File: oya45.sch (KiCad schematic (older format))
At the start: 94 parts, among them U1 ProMicro

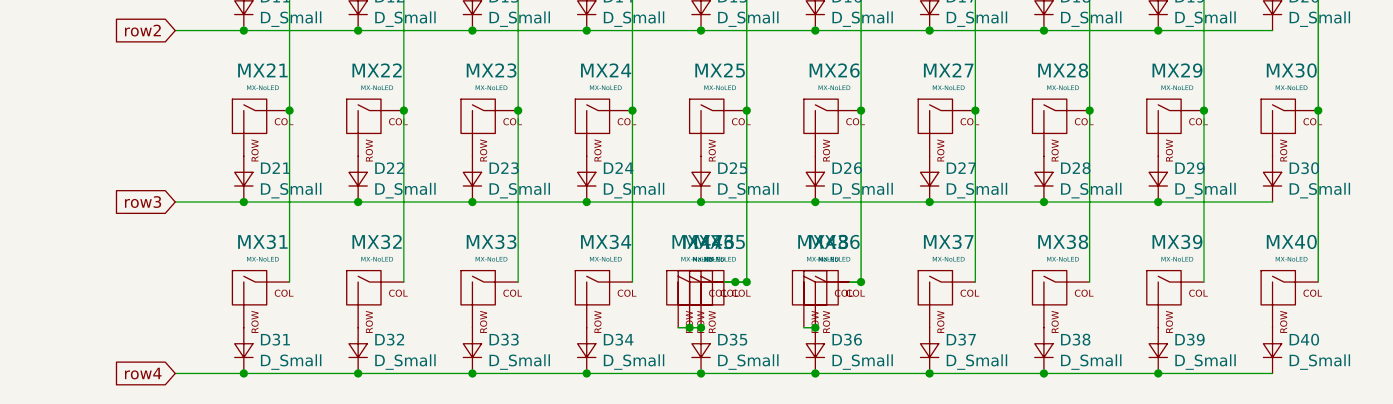
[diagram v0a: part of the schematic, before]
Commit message: schematics update
added bottom row schematics
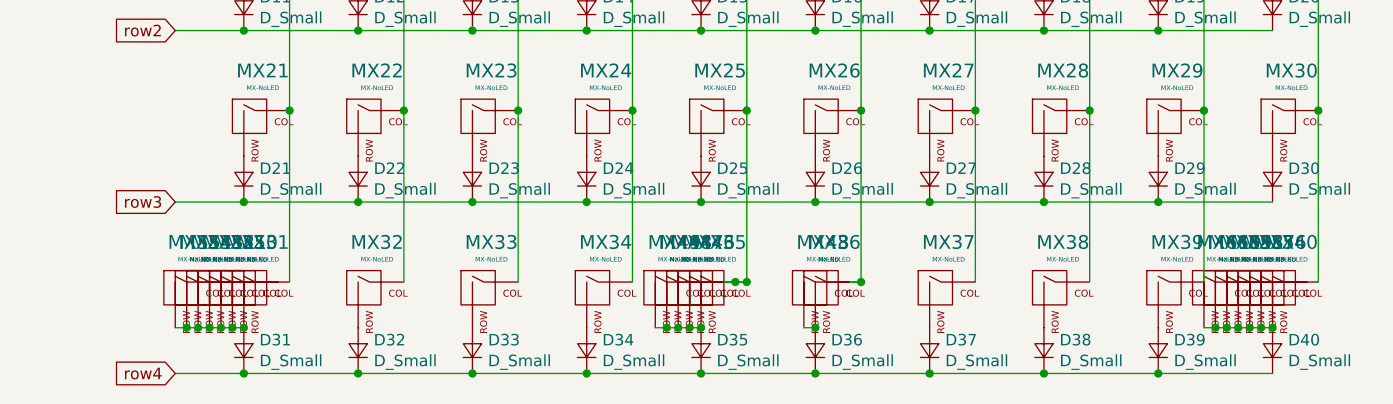
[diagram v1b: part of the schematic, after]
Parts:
- added MX48, MX49: MX-NoLED, MX_Only:MXOnly-2U-ReversedStabilizers-NoLED, symbol MX_Alps_Hybrid:MX-NoLED
- added MX50, MX51, MX52, MX53, MX54, MX55, MX56, MX57, MX58, MX59, MX60, MX61: MX-NoLED, MX_Only:MXOnly-1U-NoLED, symbol MX_Alps_Hybrid:MX-NoLED
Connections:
- net at D31.2 (A), MX31.2 (ROW): now also MX50.2 (ROW), MX51.2 (ROW), MX52.2 (ROW), MX53.2 (ROW), MX54.2 (ROW), MX55.2 (ROW)
- net at D35.2 (A), MX35.2 (ROW), MX46.2 (ROW)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: now also MX48.2 (ROW), MX49.2 (ROW)
- net at D40.2 (A), MX40.2 (ROW): now also MX56.2 (ROW), MX57.2 (ROW), MX58.2 (ROW), MX59.2 (ROW), MX60.2 (ROW), MX61.2 (ROW)
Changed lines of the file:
@@
 	7750 2550 7750 1500
 Connection ~ 7750 2550
+$Comp
+L MX_Alps_Hybrid:MX-NoLED MX50
+U 1 1 6130DEB4
+P 5550 4850
+F 0 "MX50" H 5583 5073 60  0000 C CNN
+F 1 "MX-NoLED" H 5583 4999 20  0000 C CNN
+F 2 "MX_Only:MXOnly-1U-NoLED" H 4925 4825 60  0001 C CNN
+F 3 "" H 4925 4825 60  0001 C CNN
+	1    5550 4850
+	1    0    0    -1
+$EndComp
+$Comp
+L MX_Alps_Hybrid:MX-NoLED MX51
+U 1 1 61310BF7
+P 5500 4850
+F 0 "MX51" H 5533 5073 60  0000 C CNN
+F 1 "MX-NoLED" H 5533 4999 20  0000 C CNN
+F 2 "MX_Only:MXOnly-1U-NoLED" H 4875 4825 60  0001 C CNN
+F 3 "" H 4875 4825 60  0001 C CNN
+	1    5500 4850
+	1    0    0    -1
+$EndComp
+$Comp
+L MX_Alps_Hybrid:MX-NoLED MX52
+U 1 1 6131191D
+P 5450 4850
+F 0 "MX52" H 5483 5073 60  0000 C CNN
+F 1 "MX-NoLED" H 5483 4999 20  0000 C CNN
+F 2 "MX_Only:MXOnly-1U-NoLED" H 4825 4825 60  0001 C CNN
+F 3 "" H 4825 4825 60  0001 C CNN
+	1    5450 4850
+	1    0    0    -1
+$EndComp
+$Comp
+L MX_Alps_Hybrid:MX-NoLED MX53
+U 1 1 61311AAE
+P 5400 4850
+F 0 "MX53" H 5433 5073 60  0000 C CNN
+F 1 "MX-NoLED" H 5433 4999 20  0000 C CNN
+F 2 "MX_Only:MXOnly-1U-NoLED" H 4775 4825 60  0001 C CNN
+F 3 "" H 4775 4825 60  0001 C CNN
+	1    5400 4850
+	1    0    0    -1
+$EndComp
+$Comp
+L MX_Alps_Hybrid:MX-NoLED MX54
+U 1 1 61311CE4
+P 5350 4850
+F 0 "MX54" H 5383 5073 60  0000 C CNN
+F 1 "MX-NoLED" H 5383 4999 20  0000 C CNN
+F 2 "MX_Only:MXOnly-1U-NoLED" H 4725 4825 60  0001 C CNN
+F 3 "" H 4725 4825 60  0001 C CNN
+	1    5350 4850
+	1    0    0    -1
+$EndComp
+$Comp
+L MX_Alps_Hybrid:MX-NoLED MX55
+U 1 1 61311E89
+P 5300 4850
+F 0 "MX55" H 5333 5073 60  0000 C CNN
+F 1 "MX-NoLED" H 5333 4999 20  0000 C CNN
+F 2 "MX_Only:MXOnly-1U-NoLED" H 4675 4825 60  0001 C CNN
+F 3 "" H 4675 4825 60  0001 C CNN
+	1    5300 4850
+	1    0    0    -1
+$EndComp
+$Comp
+L MX_Alps_Hybrid:MX-NoLED MX56
+U 1 1 6131203D
+P 10050 4850
+F 0 "MX56" H 10083 5073 60  0000 C CNN
+F 1 "MX-NoLED" H 10083 4999 20  0000 C CNN
+F 2 "MX_Only:MXOnly-1U-NoLED" H 9425 4825 60  0001 C CNN
+F 3 "" H 9425 4825 60  0001 C CNN
+	1    10050 4850
+	1    0    0    -1
+$EndComp
+$Comp
+L MX_Alps_Hybrid:MX-NoLED MX57
+U 1 1 6131231D
+P 10000 4850
+F 0 "MX57" H 10033 5073 60  0000 C CNN
+F 1 "MX-NoLED" H 10033 4999 20  0000 C CNN
+F 2 "MX_Only:MXOnly-1U-NoLED" H 9375 4825 60  0001 C CNN
+F 3 "" H 9375 4825 60  0001 C CNN
+	1    10000 4850
+	1    0    0    -1
+$EndComp
+$Comp
+L MX_Alps_Hybrid:MX-NoLED MX58
+U 1 1 6131254E
+P 9950 4850
+F 0 "MX58" H 9983 5073 60  0000 C CNN
+F 1 "MX-NoLED" H 9983 4999 20  0000 C CNN
+F 2 "MX_Only:MXOnly-1U-NoLED" H 9325 4825 60  0001 C CNN
+F 3 "" H 9325 4825 60  0001 C CNN
+	1    9950 4850
+	1    0    0    -1
+$EndComp
+$Comp
+L MX_Alps_Hybrid:MX-NoLED MX59
+U 1 1 6131279D
+P 9900 4850
+F 0 "MX59" H 9933 5073 60  0000 C CNN
+F 1 "MX-NoLED" H 9933 4999 20  0000 C CNN
+F 2 "MX_Only:MXOnly-1U-NoLED" H 9275 4825 60  0001 C CNN
+F 3 "" H 9275 4825 60  0001 C CNN
+	1    9900 4850
+	1    0    0    -1
+$EndComp
+$Comp
+L MX_Alps_Hybrid:MX-NoLED MX60
+U 1 1 613129F6
+P 9850 4850
+F 0 "MX60" H 9883 5073 60  0000 C CNN
+F 1 "MX-NoLED" H 9883 4999 20  0000 C CNN
+F 2 "MX_Only:MXOnly-1U-NoLED" H 9225 4825 60  0001 C CNN
+F 3 "" H 9225 4825 60  0001 C CNN
+	1    9850 4850
+	1    0    0    -1
+$EndComp
+$Comp
+L MX_Alps_Hybrid:MX-NoLED MX61
+U 1 1 61312BF5
+P 9800 4850
+F 0 "MX61" H 9833 5073 60  0000 C CNN
+F 1 "MX-NoLED" H 9833 4999 20  0000 C CNN
+F 2 "MX_Only:MXOnly-1U-NoLED" H 9175 4825 60  0001 C CNN
+F 3 "" H 9175 4825 60  0001 C CNN
+	1    9800 4850
+	1    0    0    -1
+$EndComp
+$Comp
+L MX_Alps_Hybrid:MX-NoLED MX48
+U 1 1 61316CF3
+P 7450 4850
+F 0 "MX48" H 7483 5073 60  0000 C CNN
+F 1 "MX-NoLED" H 7483 4999 20  0000 C CNN
+F 2 "MX_Only:MXOnly-2U-ReversedStabilizers-NoLED" H 6825 4825 60  0001 C CNN
+F 3 "" H 6825 4825 60  0001 C CNN
+	1    7450 4850
+	1    0    0    -1
+$EndComp
+$Comp
+L MX_Alps_Hybrid:MX-NoLED MX49
+U 1 1 61316F9C
+P 7400 4850
+F 0 "MX49" H 7433 5073 60  0000 C CNN
+F 1 "MX-NoLED" H 7433 4999 20  0000 C CNN
+F 2 "MX_Only:MXOnly-2U-ReversedStabilizers-NoLED" H 6775 4825 60  0001 C CNN
+F 3 "" H 6775 4825 60  0001 C CNN
+	1    7400 4850
+	1    0    0    -1
+$EndComp
+Wire Wire Line
+	7450 5000 7400 5000
+Connection ~ 7450 5000
+Connection ~ 7400 5000
+Wire Wire Line
+	7400 5000 7350 5000
+Connection ~ 5550 5000
+Wire Wire Line
+	5300 5000 5250 5000
+Connection ~ 5300 5000
+Wire Wire Line
+	5350 5000 5300 5000
+Connection ~ 5350 5000
+Wire Wire Line
+	5400 5000 5350 5000
+Connection ~ 5400 5000
+Wire Wire Line
+	5450 5000 5400 5000
+Connection ~ 5450 5000
+Wire Wire Line
+	5550 5000 5500 5000
+Wire Wire Line
+	5500 5000 5450 5000
+Connection ~ 5500 5000
+Connection ~ 10050 5000
+Wire Wire Line
+	9800 5000 9750 5000
+Connection ~ 9800 5000
+Wire Wire Line
+	9850 5000 9800 5000
+Connection ~ 9850 5000
+Wire Wire Line
+	9900 5000 9850 5000
+Connection ~ 9900 5000
+Wire Wire Line
+	9950 5000 9900 5000
+Connection ~ 9950 5000
+Wire Wire Line
+	10050 5000 10000 5000
+Wire Wire Line
+	10000 5000 9950 5000
+Connection ~ 10000 5000
 $EndSCHEMATC

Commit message: fixed schematic
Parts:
- renumbered MX48 to MX49, MX49 to MX50, MX50 to MX51, MX51 to MX52, MX52 to MX53, MX53 to MX54, MX54 to MX55, MX55 to MX56, MX56 to MX57, MX57 to MX58, MX58 to MX59, MX59 to MX60, MX60 to MX61, MX61 to MX62
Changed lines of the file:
@@
 Connection ~ 7750 2550
 $Comp
-L MX_Alps_Hybrid:MX-NoLED MX50
-U 1 1 6130DEB4
-P 5550 4850
-F 0 "MX50" H 5583 5073 60  0000 C CNN
-F 1 "MX-NoLED" H 5583 4999 20  0000 C CNN
-F 2 "MX_Only:MXOnly-1U-NoLED" H 4925 4825 60  0001 C CNN
-F 3 "" H 4925 4825 60  0001 C CNN
-	1    5550 4850
-	1    0    0    -1
-$EndComp
-$Comp
-L MX_Alps_Hybrid:MX-NoLED MX51
-U 1 1 61310BF7
-P 5500 4850
-F 0 "MX51" H 5533 5073 60  0000 C CNN
-F 1 "MX-NoLED" H 5533 4999 20  0000 C CNN
-F 2 "MX_Only:MXOnly-1U-NoLED" H 4875 4825 60  0001 C CNN
-F 3 "" H 4875 4825 60  0001 C CNN
-	1    5500 4850
-	1    0    0    -1
-$EndComp
-$Comp
-L MX_Alps_Hybrid:MX-NoLED MX52
-U 1 1 6131191D
-P 5450 4850
-F 0 "MX52" H 5483 5073 60  0000 C CNN
-F 1 "MX-NoLED" H 5483 4999 20  0000 C CNN
-F 2 "MX_Only:MXOnly-1U-NoLED" H 4825 4825 60  0001 C CNN
-F 3 "" H 4825 4825 60  0001 C CNN
-	1    5450 4850
-	1    0    0    -1
-$EndComp
-$Comp
-L MX_Alps_Hybrid:MX-NoLED MX53
+L MX_Alps_Hybrid:MX-NoLED MX54
 U 1 1 61311AAE
 P 5400 4850
-F 0 "MX53" H 5433 5073 60  0000 C CNN
+F 0 "MX54" H 5433 5073 60  0000 C CNN
 F 1 "MX-NoLED" H 5433 4999 20  0000 C CNN
 F 2 "MX_Only:MXOnly-1U-NoLED" H 4775 4825 60  0001 C CNN
@@
 $EndComp
 $Comp
-L MX_Alps_Hybrid:MX-NoLED MX54
+L MX_Alps_Hybrid:MX-NoLED MX55
 U 1 1 61311CE4
 P 5350 4850
-F 0 "MX54" H 5383 5073 60  0000 C CNN
+F 0 "MX55" H 5383 5073 60  0000 C CNN
 F 1 "MX-NoLED" H 5383 4999 20  0000 C CNN
 F 2 "MX_Only:MXOnly-1U-NoLED" H 4725 4825 60  0001 C CNN
@@
 $EndComp
 $Comp
-L MX_Alps_Hybrid:MX-NoLED MX55
+L MX_Alps_Hybrid:MX-NoLED MX56
 U 1 1 61311E89
 P 5300 4850
-F 0 "MX55" H 5333 5073 60  0000 C CNN
+F 0 "MX56" H 5333 5073 60  0000 C CNN
 F 1 "MX-NoLED" H 5333 4999 20  0000 C CNN
 F 2 "MX_Only:MXOnly-1U-NoLED" H 4675 4825 60  0001 C CNN
@@
 $EndComp
 $Comp
-L MX_Alps_Hybrid:MX-NoLED MX56
+L MX_Alps_Hybrid:MX-NoLED MX57
 U 1 1 6131203D
 P 10050 4850
-F 0 "MX56" H 10083 5073 60  0000 C CNN
+F 0 "MX57" H 10083 5073 60  0000 C CNN
 F 1 "MX-NoLED" H 10083 4999 20  0000 C CNN
 F 2 "MX_Only:MXOnly-1U-NoLED" H 9425 4825 60  0001 C CNN
@@
 $EndComp
 $Comp
-L MX_Alps_Hybrid:MX-NoLED MX57
+L MX_Alps_Hybrid:MX-NoLED MX58
 U 1 1 6131231D
 P 10000 4850
-F 0 "MX57" H 10033 5073 60  0000 C CNN
+F 0 "MX58" H 10033 5073 60  0000 C CNN
 F 1 "MX-NoLED" H 10033 4999 20  0000 C CNN
 F 2 "MX_Only:MXOnly-1U-NoLED" H 9375 4825 60  0001 C CNN
@@
 $EndComp
 $Comp
-L MX_Alps_Hybrid:MX-NoLED MX58
+L MX_Alps_Hybrid:MX-NoLED MX59
 U 1 1 6131254E
 P 9950 4850
-F 0 "MX58" H 9983 5073 60  0000 C CNN
+F 0 "MX59" H 9983 5073 60  0000 C CNN
 F 1 "MX-NoLED" H 9983 4999 20  0000 C CNN
 F 2 "MX_Only:MXOnly-1U-NoLED" H 9325 4825 60  0001 C CNN
@@
 $EndComp
 $Comp
-L MX_Alps_Hybrid:MX-NoLED MX59
+L MX_Alps_Hybrid:MX-NoLED MX60
 U 1 1 6131279D
 P 9900 4850
-F 0 "MX59" H 9933 5073 60  0000 C CNN
+F 0 "MX60" H 9933 5073 60  0000 C CNN
 F 1 "MX-NoLED" H 9933 4999 20  0000 C CNN
 F 2 "MX_Only:MXOnly-1U-NoLED" H 9275 4825 60  0001 C CNN
@@
 $EndComp
 $Comp
-L MX_Alps_Hybrid:MX-NoLED MX60
+L MX_Alps_Hybrid:MX-NoLED MX61
 U 1 1 613129F6
 P 9850 4850
-F 0 "MX60" H 9883 5073 60  0000 C CNN
+F 0 "MX61" H 9883 5073 60  0000 C CNN
 F 1 "MX-NoLED" H 9883 4999 20  0000 C CNN
 F 2 "MX_Only:MXOnly-1U-NoLED" H 9225 4825 60  0001 C CNN
@@
 $EndComp
 $Comp
-L MX_Alps_Hybrid:MX-NoLED MX61
+L MX_Alps_Hybrid:MX-NoLED MX62
 U 1 1 61312BF5
 P 9800 4850
-F 0 "MX61" H 9833 5073 60  0000 C CNN
+F 0 "MX62" H 9833 5073 60  0000 C CNN
 F 1 "MX-NoLED" H 9833 4999 20  0000 C CNN
 F 2 "MX_Only:MXOnly-1U-NoLED" H 9175 4825 60  0001 C CNN
@@
 $EndComp
 $Comp
-L MX_Alps_Hybrid:MX-NoLED MX48
+L MX_Alps_Hybrid:MX-NoLED MX49
 U 1 1 61316CF3
 P 7450 4850
-F 0 "MX48" H 7483 5073 60  0000 C CNN
+F 0 "MX49" H 7483 5073 60  0000 C CNN
 F 1 "MX-NoLED" H 7483 4999 20  0000 C CNN
 F 2 "MX_Only:MXOnly-2U-ReversedStabilizers-NoLED" H 6825 4825 60  0001 C CNN
@@
 $EndComp
 $Comp
-L MX_Alps_Hybrid:MX-NoLED MX49
+L MX_Alps_Hybrid:MX-NoLED MX50
 U 1 1 61316F9C
 P 7400 4850
-F 0 "MX49" H 7433 5073 60  0000 C CNN
+F 0 "MX50" H 7433 5073 60  0000 C CNN
 F 1 "MX-NoLED" H 7433 4999 20  0000 C CNN
 F 2 "MX_Only:MXOnly-2U-ReversedStabilizers-NoLED" H 6775 4825 60  0001 C CNN
@@
 Wire Wire Line
 	7400 5000 7350 5000
-Connection ~ 5550 5000
 Wire Wire Line
 	5300 5000 5250 5000
@@
 	5400 5000 5350 5000
 Connection ~ 5400 5000
-Wire Wire Line
-	5450 5000 5400 5000
-Connection ~ 5450 5000
-Wire Wire Line
-	5550 5000 5500 5000
-Wire Wire Line
-	5500 5000 5450 5000
-Connection ~ 5500 5000
 Connection ~ 10050 5000
 Wire Wire Line
@@
 	10000 5000 9950 5000
 Connection ~ 10000 5000
+Connection ~ 5550 5000
+Connection ~ 5450 5000
+Wire Wire Line
+	5450 5000 5400 5000
+$Comp
+L MX_Alps_Hybrid:MX-NoLED MX52
+U 1 1 61310BF7
+P 5500 4850
+F 0 "MX52" H 5533 5073 60  0000 C CNN
+F 1 "MX-NoLED" H 5533 4999 20  0000 C CNN
+F 2 "MX_Only:MXOnly-1U-NoLED" H 4875 4825 60  0001 C CNN
+F 3 "" H 4875 4825 60  0001 C CNN
+	1    5500 4850
+	1    0    0    -1
+$EndComp
+Connection ~ 5500 5000
+Wire Wire Line
+	5500 5000 5450 5000
+Wire Wire Line
+	5550 5000 5500 5000
+$Comp
+L MX_Alps_Hybrid:MX-NoLED MX51
+U 1 1 6130DEB4
+P 5550 4850
+F 0 "MX51" H 5583 5073 60  0000 C CNN
+F 1 "MX-NoLED" H 5583 4999 20  0000 C CNN
+F 2 "MX_Only:MXOnly-1U-NoLED" H 4925 4825 60  0001 C CNN
+F 3 "" H 4925 4825 60  0001 C CNN
+	1    5550 4850
+	1    0    0    -1
+$EndComp
+$Comp
+L MX_Alps_Hybrid:MX-NoLED MX53
+U 1 1 6131191D
+P 5450 4850
+F 0 "MX53" H 5483 5073 60  0000 C CNN
+F 1 "MX-NoLED" H 5483 4999 20  0000 C CNN
+F 2 "MX_Only:MXOnly-1U-NoLED" H 4825 4825 60  0001 C CNN
+F 3 "" H 4825 4825 60  0001 C CNN
+	1    5450 4850
+	1    0    0    -1
+$EndComp
 $EndSCHEMATC

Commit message: finish schematics
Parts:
- MX49: footprint MX_Only:MXOnly-2U-ReversedStabilizers-NoLED -> MX_Only:MXOnly-6.25U-ReversedStabilizers-NoLED
- MX50: footprint MX_Only:MXOnly-2U-ReversedStabilizers-NoLED -> MX_Only:MXOnly-7U-ReversedStabilizers-NoLED
- MX51, MX52, MX53, MX57, MX58, MX59: footprint MX_Only:MXOnly-1U-NoLED -> MX_Only:MXOnly-1.25U-NoLED
- MX54, MX55, MX56, MX60, MX61, MX62: footprint MX_Only:MXOnly-1U-NoLED -> MX_Only:MXOnly-1.5U-NoLED
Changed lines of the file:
@@
 F 0 "MX54" H 5433 5073 60  0000 C CNN
 F 1 "MX-NoLED" H 5433 4999 20  0000 C CNN
-F 2 "MX_Only:MXOnly-1U-NoLED" H 4775 4825 60  0001 C CNN
+F 2 "MX_Only:MXOnly-1.5U-NoLED" H 4775 4825 60  0001 C CNN
 F 3 "" H 4775 4825 60  0001 C CNN
 	1    5400 4850
@@
 F 0 "MX55" H 5383 5073 60  0000 C CNN
 F 1 "MX-NoLED" H 5383 4999 20  0000 C CNN
-F 2 "MX_Only:MXOnly-1U-NoLED" H 4725 4825 60  0001 C CNN
+F 2 "MX_Only:MXOnly-1.5U-NoLED" H 4725 4825 60  0001 C CNN
 F 3 "" H 4725 4825 60  0001 C CNN
 	1    5350 4850
@@
 F 0 "MX56" H 5333 5073 60  0000 C CNN
 F 1 "MX-NoLED" H 5333 4999 20  0000 C CNN
-F 2 "MX_Only:MXOnly-1U-NoLED" H 4675 4825 60  0001 C CNN
+F 2 "MX_Only:MXOnly-1.5U-NoLED" H 4675 4825 60  0001 C CNN
 F 3 "" H 4675 4825 60  0001 C CNN
 	1    5300 4850
@@
 F 0 "MX57" H 10083 5073 60  0000 C CNN
 F 1 "MX-NoLED" H 10083 4999 20  0000 C CNN
-F 2 "MX_Only:MXOnly-1U-NoLED" H 9425 4825 60  0001 C CNN
+F 2 "MX_Only:MXOnly-1.25U-NoLED" H 9425 4825 60  0001 C CNN
 F 3 "" H 9425 4825 60  0001 C CNN
 	1    10050 4850
@@
 F 0 "MX58" H 10033 5073 60  0000 C CNN
 F 1 "MX-NoLED" H 10033 4999 20  0000 C CNN
-F 2 "MX_Only:MXOnly-1U-NoLED" H 9375 4825 60  0001 C CNN
+F 2 "MX_Only:MXOnly-1.25U-NoLED" H 9375 4825 60  0001 C CNN
 F 3 "" H 9375 4825 60  0001 C CNN
 	1    10000 4850
@@
 F 0 "MX59" H 9983 5073 60  0000 C CNN
 F 1 "MX-NoLED" H 9983 4999 20  0000 C CNN
-F 2 "MX_Only:MXOnly-1U-NoLED" H 9325 4825 60  0001 C CNN
+F 2 "MX_Only:MXOnly-1.25U-NoLED" H 9325 4825 60  0001 C CNN
 F 3 "" H 9325 4825 60  0001 C CNN
 	1    9950 4850
@@
 F 0 "MX60" H 9933 5073 60  0000 C CNN
 F 1 "MX-NoLED" H 9933 4999 20  0000 C CNN
-F 2 "MX_Only:MXOnly-1U-NoLED" H 9275 4825 60  0001 C CNN
+F 2 "MX_Only:MXOnly-1.5U-NoLED" H 9275 4825 60  0001 C CNN
 F 3 "" H 9275 4825 60  0001 C CNN
 	1    9900 4850
@@
 F 0 "MX61" H 9883 5073 60  0000 C CNN
 F 1 "MX-NoLED" H 9883 4999 20  0000 C CNN
-F 2 "MX_Only:MXOnly-1U-NoLED" H 9225 4825 60  0001 C CNN
+F 2 "MX_Only:MXOnly-1.5U-NoLED" H 9225 4825 60  0001 C CNN
 F 3 "" H 9225 4825 60  0001 C CNN
 	1    9850 4850
@@
 F 0 "MX62" H 9833 5073 60  0000 C CNN
 F 1 "MX-NoLED" H 9833 4999 20  0000 C CNN
-F 2 "MX_Only:MXOnly-1U-NoLED" H 9175 4825 60  0001 C CNN
+F 2 "MX_Only:MXOnly-1.5U-NoLED" H 9175 4825 60  0001 C CNN
 F 3 "" H 9175 4825 60  0001 C CNN
 	1    9800 4850
@@
 F 0 "MX49" H 7483 5073 60  0000 C CNN
 F 1 "MX-NoLED" H 7483 4999 20  0000 C CNN
-F 2 "MX_Only:MXOnly-2U-ReversedStabilizers-NoLED" H 6825 4825 60  0001 C CNN
+F 2 "MX_Only:MXOnly-6.25U-ReversedStabilizers-NoLED" H 6825 4825 60  0001 C CNN
 F 3 "" H 6825 4825 60  0001 C CNN
 	1    7450 4850
@@
 F 0 "MX50" H 7433 5073 60  0000 C CNN
 F 1 "MX-NoLED" H 7433 4999 20  0000 C CNN
-F 2 "MX_Only:MXOnly-2U-ReversedStabilizers-NoLED" H 6775 4825 60  0001 C CNN
+F 2 "MX_Only:MXOnly-7U-ReversedStabilizers-NoLED" H 6775 4825 60  0001 C CNN
 F 3 "" H 6775 4825 60  0001 C CNN
 	1    7400 4850
@@
 F 0 "MX52" H 5533 5073 60  0000 C CNN
 F 1 "MX-NoLED" H 5533 4999 20  0000 C CNN
-F 2 "MX_Only:MXOnly-1U-NoLED" H 4875 4825 60  0001 C CNN
+F 2 "MX_Only:MXOnly-1.25U-NoLED" H 4875 4825 60  0001 C CNN
 F 3 "" H 4875 4825 60  0001 C CNN
 	1    5500 4850
@@
 F 0 "MX51" H 5583 5073 60  0000 C CNN
 F 1 "MX-NoLED" H 5583 4999 20  0000 C CNN
-F 2 "MX_Only:MXOnly-1U-NoLED" H 4925 4825 60  0001 C CNN
+F 2 "MX_Only:MXOnly-1.25U-NoLED" H 4925 4825 60  0001 C CNN
 F 3 "" H 4925 4825 60  0001 C CNN
 	1    5550 4850
@@
 F 0 "MX53" H 5483 5073 60  0000 C CNN
 F 1 "MX-NoLED" H 5483 4999 20  0000 C CNN
-F 2 "MX_Only:MXOnly-1U-NoLED" H 4825 4825 60  0001 C CNN
+F 2 "MX_Only:MXOnly-1.25U-NoLED" H 4825 4825 60  0001 C CNN
 F 3 "" H 4825 4825 60  0001 C CNN
 	1    5450 4850
